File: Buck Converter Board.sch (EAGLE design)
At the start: 4 parts

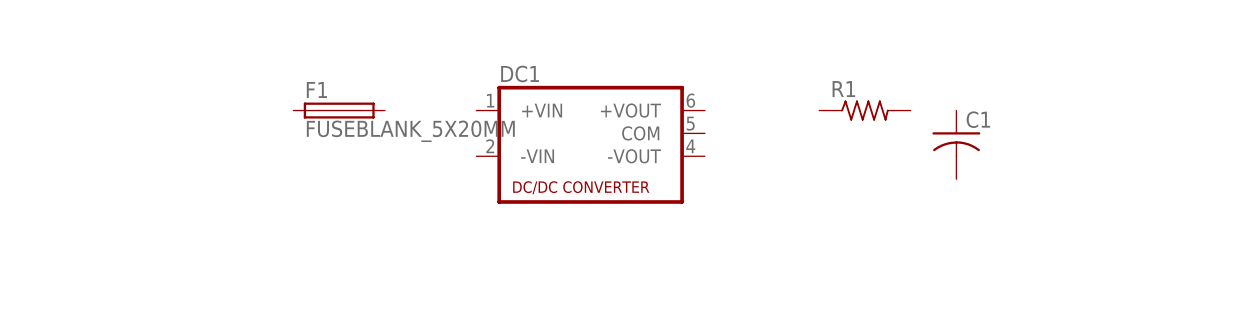
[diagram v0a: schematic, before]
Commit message: created buck converter board
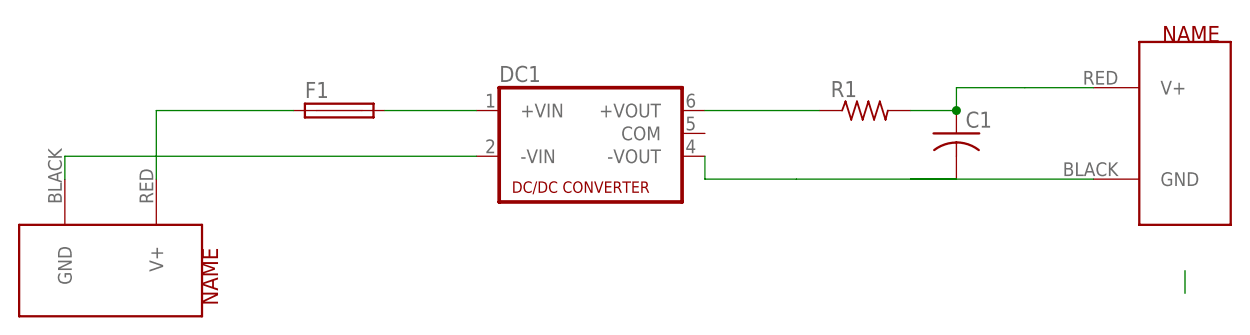
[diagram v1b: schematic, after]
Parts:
- added J1, J2: POWERPOLE_POWER25A_HORIZONTAL_G2, powerpoles:POWERPOLE_POWER25A_HORIZONTAL_G2
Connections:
- new net N$1: F1.1, J1.V+
- new net N$2: DC1.+VIN, F1.2
- new net N$3: DC1.-VIN, J1.GND
- new net N$4: DC1.+VOUT, R1.1
- new net N$5: C1.1, J2.V+, R1.2
- new net N$6: C1.2, DC1.-VOUT, J2.GND
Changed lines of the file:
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@@
 <part name="R1" library="rcl" library_urn="urn:adsk.eagle:library:334" deviceset="R-US_" device="R0805" package3d_urn="urn:adsk.eagle:package:23553/2"/>
 <part name="C1" library="rcl" library_urn="urn:adsk.eagle:library:334" deviceset="C-US" device="C0805" package3d_urn="urn:adsk.eagle:package:23617/2"/>
+<part name="J1" library="powerpoles" deviceset="POWERPOLE_POWER" device="25A_HORIZONTAL_G2"/>
+<part name="J2" library="powerpoles" deviceset="POWERPOLE_POWER" device="25A_HORIZONTAL_G2"/>
 </parts>
 <sheets>
@@
 <instances>
 <instance part="DC1" gate="G$1" x="60.96" y="58.42"/>
-<instance part="F1" gate="G$1" x="33.02" y="60.96"/>
+<instance part="F1" gate="G$1" x="33.02" y="60.96" smashed="yes">
+<attribute name="NAME" x="29.21" y="62.357" size="1.778" layer="95"/>
+</instance>
 <instance part="R1" gate="G$1" x="91.44" y="60.96"/>
 <instance part="C1" gate="G$1" x="101.6" y="58.42"/>
+<instance part="J1" gate="G$1" x="7.62" y="43.18" rot="R270"/>
+<instance part="J2" gate="G$1" x="127" y="58.42"/>
 </instances>
 <busses>
 </busses>
 <nets>
+<net name="N$1" class="0">
+<segment>
+<pinref part="J1" gate="G$1" pin="V+"/>
+<pinref part="F1" gate="G$1" pin="1"/>
+<wire x1="12.7" y1="53.34" x2="12.7" y2="60.96" width="0.1524" layer="91"/>
+<wire x1="12.7" y1="60.96" x2="27.94" y2="60.96" width="0.1524" layer="91"/>
+</segment>
+</net>
+<net name="N$2" class="0">
+<segment>
+<pinref part="F1" gate="G$1" pin="2"/>
+<pinref part="DC1" gate="G$1" pin="+VIN"/>
+<wire x1="38.1" y1="60.96" x2="48.26" y2="60.96" width="0.1524" layer="91"/>
+</segment>
+</net>
+<net name="N$3" class="0">
+<segment>
+<pinref part="J1" gate="G$1" pin="GND"/>
+<pinref part="DC1" gate="G$1" pin="-VIN"/>
+<wire x1="2.54" y1="53.34" x2="2.54" y2="55.88" width="0.1524" layer="91"/>
+<wire x1="2.54" y1="55.88" x2="48.26" y2="55.88" width="0.1524" layer="91"/>
+</segment>
+</net>
+<net name="N$4" class="0">
+<segment>
+<pinref part="DC1" gate="G$1" pin="+VOUT"/>
+<pinref part="R1" gate="G$1" pin="1"/>
+<wire x1="73.66" y1="60.96" x2="86.36" y2="60.96" width="0.1524" layer="91"/>
+</segment>
+</net>
+<net name="N$5" class="0">
+<segment>
+<pinref part="R1" gate="G$1" pin="2"/>
+<pinref part="C1" gate="G$1" pin="1"/>
+<wire x1="96.52" y1="60.96" x2="101.6" y2="60.96" width="0.1524" layer="91"/>
+<pinref part="J2" gate="G$1" pin="V+"/>
+<wire x1="101.6" y1="60.96" x2="101.6" y2="63.5" width="0.1524" layer="91"/>
+<wire x1="101.6" y1="63.5" x2="109.22" y2="63.5" width="0.1524" layer="91"/>
+<junction x="101.6" y="60.96"/>
+<wire x1="109.22" y1="63.5" x2="116.84" y2="63.5" width="0.1524" layer="91"/>
+</segment>
+</net>
+<net name="N$6" class="0">
+<segment>
+<pinref part="C1" gate="G$1" pin="2"/>
+<wire x1="101.6" y1="53.34" x2="96.52" y2="53.34" width="0.1524" layer="91"/>
+<pinref part="DC1" gate="G$1" pin="-VOUT"/>
+<wire x1="96.52" y1="53.34" x2="83.82" y2="53.34" width="0.1524" layer="91"/>
+<wire x1="83.82" y1="53.34" x2="73.66" y2="53.34" width="0.1524" layer="91"/>
+<wire x1="73.66" y1="53.34" x2="73.66" y2="55.88" width="0.1524" layer="91"/>
+<pinref part="J2" gate="G$1" pin="GND"/>
+<wire x1="116.84" y1="53.34" x2="96.52" y2="53.34" width="0.1524" layer="91"/>
+</segment>
+</net>
+<net name="N$7" class="0">
+<segment>
+<wire x1="127" y1="40.64" x2="127" y2="43.18" width="0.1524" layer="91"/>
+</segment>
+</net>
 </nets>
 </sheet>
